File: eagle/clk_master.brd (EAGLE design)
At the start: 76.2 x 50.8 mm, 68 parts

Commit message: update eagle files
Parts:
- renumbered E$1 to R13, E$11 to U4, E$12 to J1, E$13 to C1, E$14 to C2, E$15 to C3, E$16 to C4, E$17 to R1, E$18 to R2, E$19 to R3, E$2 to U3, E$20 to R4, E$21 to C5, E$22 to U7, E$23 to C26, E$24 to C25, E$25 to R15, E$26 to R14, E$27 to C27, E$28 to U6, E$29 to C29, E$3 to U9, E$30 to C28, E$31 to J2, E$32 to C13, E$33 to L1, E$34 to C14, E$35 to C31, E$36 to C30, E$37 to C6, E$38 to C9, E$39 to C7, E$4 to U2, E$40 to C8, E$41 to C10, E$42 to C17, E$43 to C11, E$44 to C12, E$45 to C18, E$47 to C19, E$48 to C15, E$49 to D2, E$5 to U8, E$50 to D1, E$51 to R5, E$52 to R6, E$53 to C22, E$54 to L3, E$55 to C23, E$56 to U5, E$57 to C24, E$58 to PDI, E$59 to R8, E$6 to U1, E$60 to R7, E$61 to R10, E$62 to R9, E$63 to C20, E$64 to C21, E$65 to L2, E$66 to C16, E$67 to R11, E$68 to R12
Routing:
- net GND: track 120.0 -> 121.0 mm

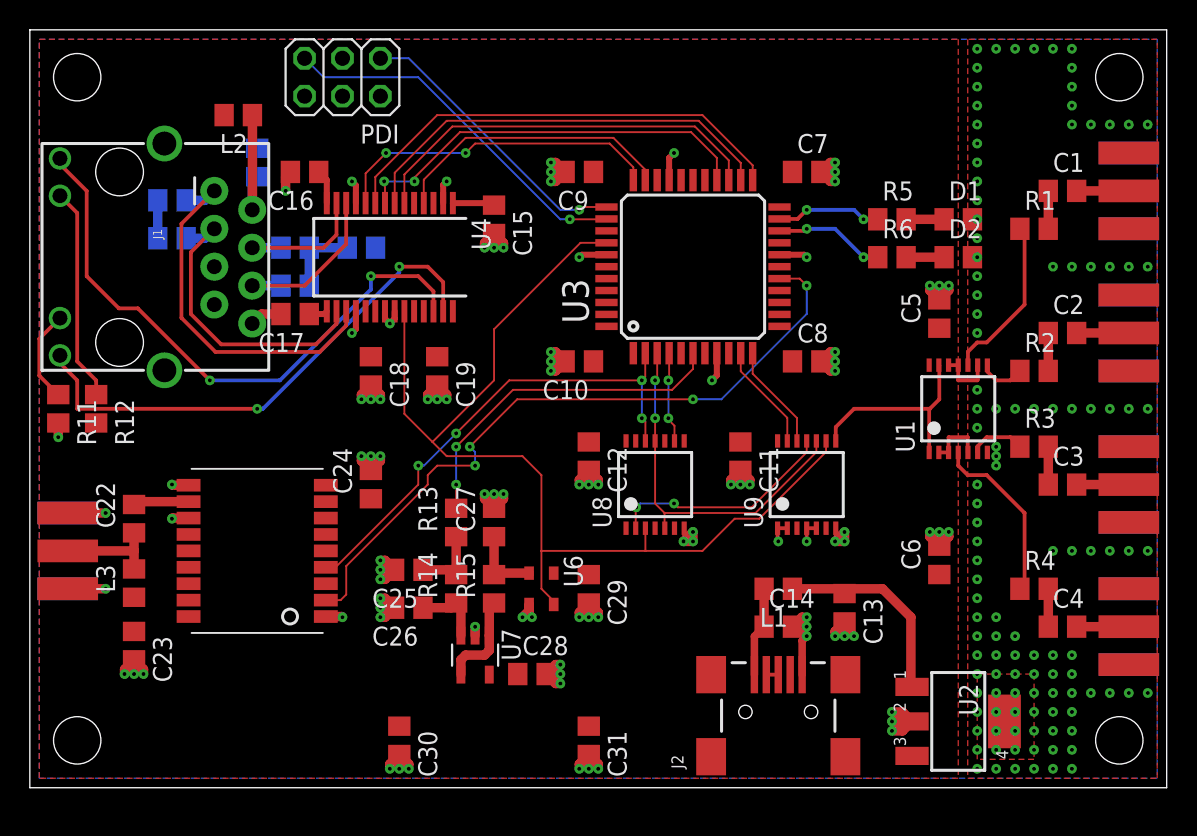
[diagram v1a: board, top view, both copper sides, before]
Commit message: clean up master clock board layout
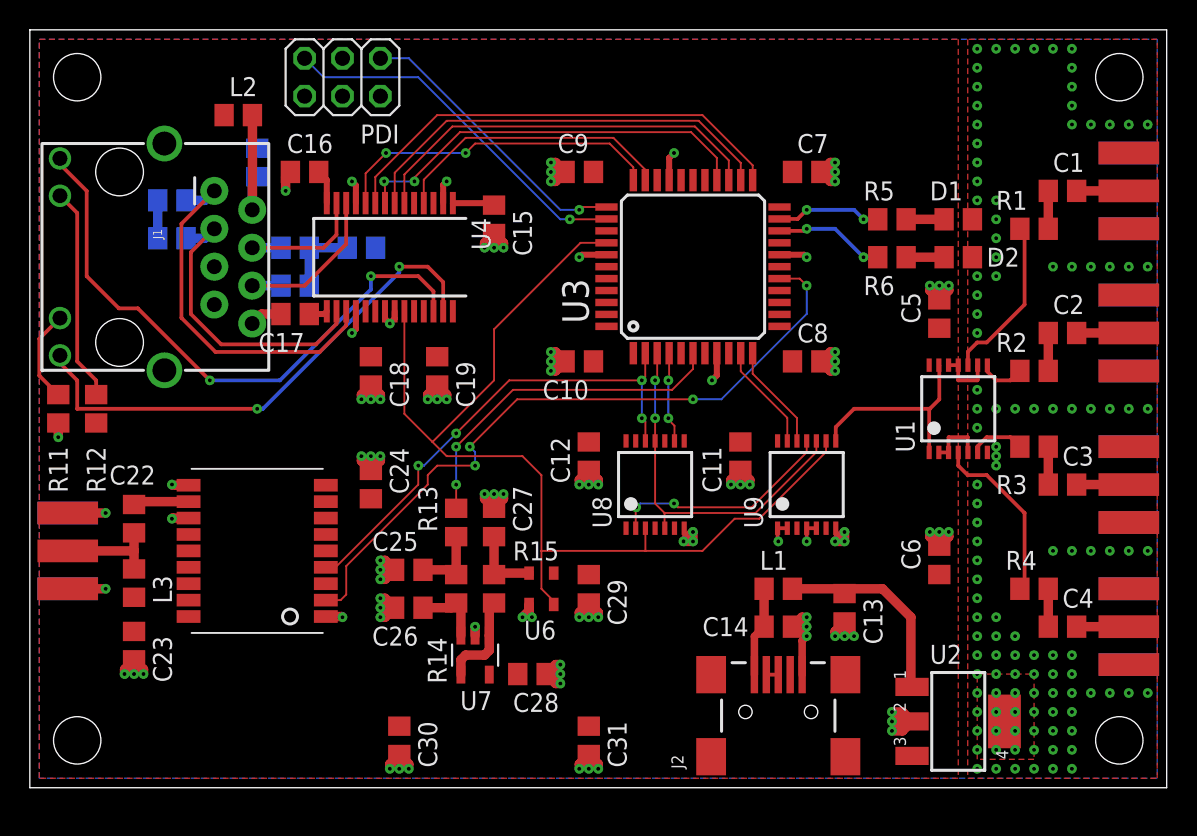
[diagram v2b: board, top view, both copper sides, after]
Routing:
- net GND: vias 209 -> 211

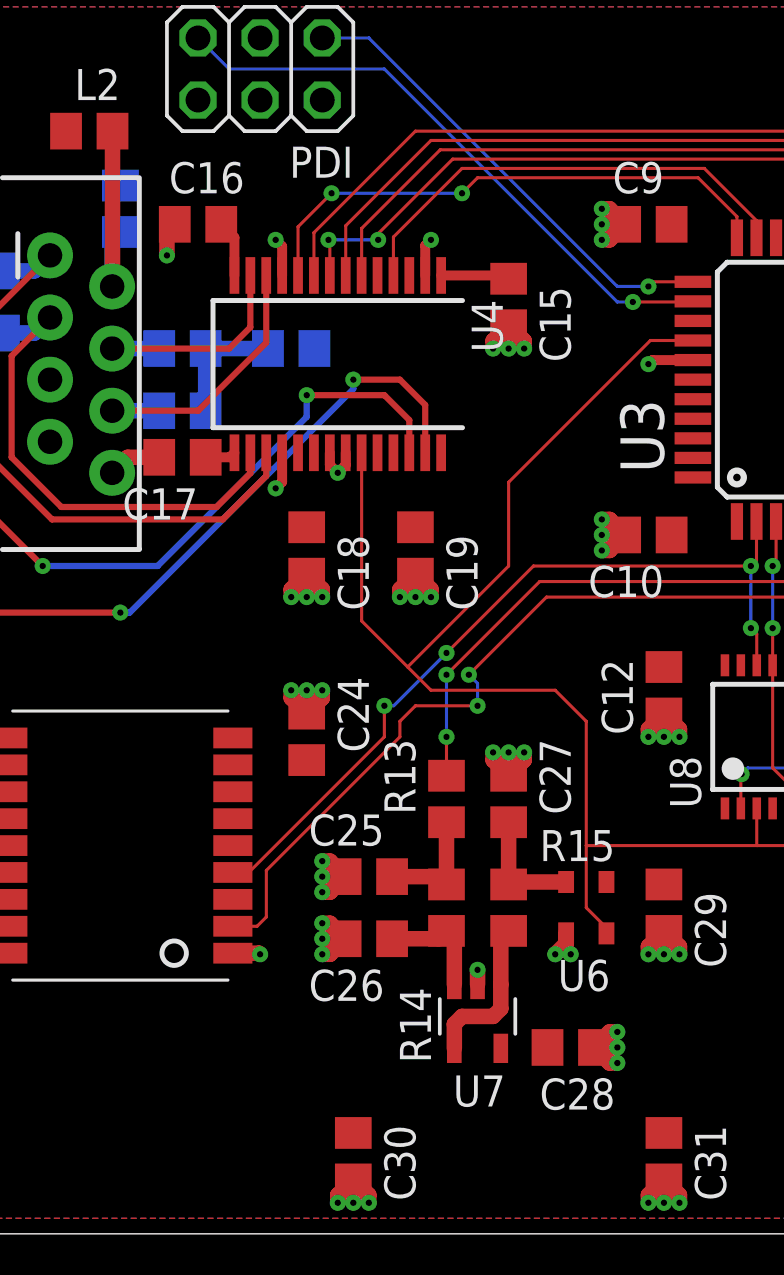
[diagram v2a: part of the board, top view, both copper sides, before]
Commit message: cleanup master clock layout
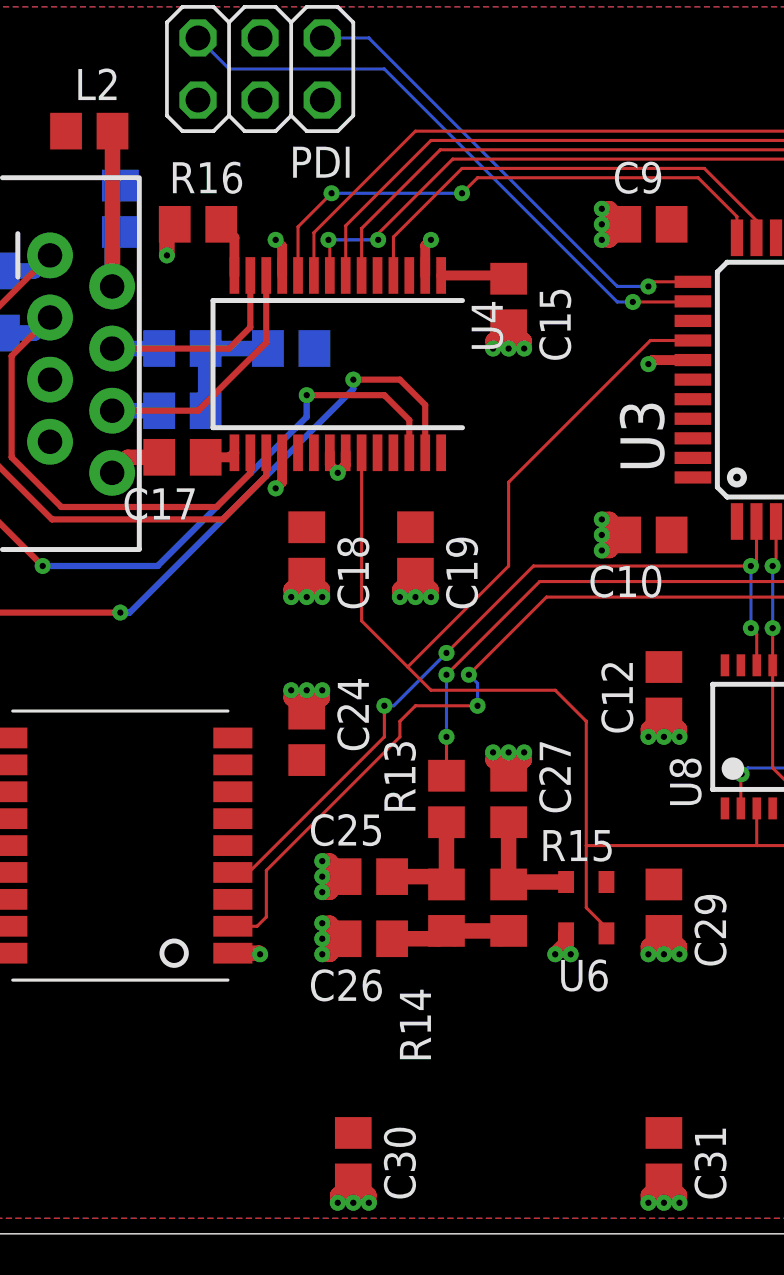
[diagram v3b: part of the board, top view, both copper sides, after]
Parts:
- removed C28: (no value), rcl:R0805
- removed U7: (no value), linear:SOT23-5
- renumbered C16 to R16
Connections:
- removed net S$19: R15.1, U7.1, U7.4
- net GND: no longer C28.2, U7.2
- net S$16: now also R15.1; no longer U7.3
- net V3.3: no longer C28.1, U7.5
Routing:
- net S$19: track 6.46 -> 0.00 mm
- net GND: track 121.0 -> 117.0 mm, vias 211 -> 207
- net S$16: track 4.68 -> 5.80 mm
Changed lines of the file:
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@@
 <attribute name="VALUE" x="63.5" y="31.115" size="1.27" layer="27" rot="R90"/>
-</element>
-<element name="U7" library="linear" library_urn="urn:adsk.eagle:library:262" package="SOT23-5" package3d_urn="urn:adsk.eagle:package:16456/2" value="" x="29.845" y="8.89" smashed="yes" rot="R180">
-<attribute name="NAME" x="30.988" y="6.477" size="1.27" layer="25" ratio="10" rot="R180"/>
-<attribute name="VALUE" x="26.797" y="10.668" size="1.27" layer="27" ratio="10" rot="R270"/>
 </element>
 <element name="C26" library="rcl" library_urn="urn:adsk.eagle:library:334" package="R0805" package3d_urn="urn:adsk.eagle:package:23553/2" value="" x="25.4" y="12.065" smashed="yes" rot="R180">
@@
 <attribute name="NAME" x="38.735" y="13.97" size="1.27" layer="25" rot="R270"/>
 <attribute name="VALUE" x="34.925" y="13.97" size="1.27" layer="27" rot="R270"/>
-</element>
-<element name="C28" library="rcl" library_urn="urn:adsk.eagle:library:334" package="R0805" package3d_urn="urn:adsk.eagle:package:23553/2" value="" x="33.655" y="7.62" smashed="yes">
-<attribute name="NAME" x="32.385" y="5.08" size="1.27" layer="25"/>
-<attribute name="VALUE" x="33.02" y="5.08" size="1.27" layer="27"/>
 </element>
 <element name="J2" library="SparkFun-Connectors" library_urn="urn:adsk.eagle:library:513" package="USB-MINIB" package3d_urn="urn:adsk.eagle:package:38244/1" value="" x="50.165" y="5.08" smashed="yes" rot="R90">
@@
 <attribute name="VALUE" x="14.605" y="47.625" size="1.27" layer="27" rot="R180"/>
 </element>
-<element name="C16" library="rcl" library_urn="urn:adsk.eagle:library:334" package="R0805" package3d_urn="urn:adsk.eagle:package:23553/2" value="" x="18.415" y="41.275" smashed="yes" rot="R180">
+<element name="R16" library="rcl" library_urn="urn:adsk.eagle:library:334" package="R0805" package3d_urn="urn:adsk.eagle:package:23553/2" value="" x="18.415" y="41.275" smashed="yes" rot="R180">
 <attribute name="NAME" x="20.32" y="43.815" size="1.27" layer="25" rot="R180"/>
 <attribute name="VALUE" x="19.05" y="43.815" size="1.27" layer="27" rot="R180"/>
@@
 <contactref element="C29" pad="1"/>
 <contactref element="U6" pad="4"/>
-<contactref element="U7" pad="5"/>
-<contactref element="C28" pad="1"/>
 <contactref element="U2" pad="3"/>
 <contactref element="C30" pad="1"/>
@@
 <wire x1="31.115" y1="18.73" x2="31.75" y2="19.365" width="0.635" layer="1"/>
 <wire x1="31.75" y1="19.365" x2="31.75" y2="19.685" width="0.635" layer="1"/>
-<via x="29.845" y="10.795" extent="1-16" drill="0.254"/>
-<contactref element="U7" pad="2"/>
-<wire x1="29.845" y1="10.196" x2="29.845" y2="10.795" width="0.635" layer="1"/>
-<contactref element="C28" pad="2"/>
-<via x="35.56" y="8.255" extent="1-16" drill="0.254"/>
-<via x="35.56" y="7.62" extent="1-16" drill="0.254"/>
-<via x="35.56" y="6.985" extent="1-16" drill="0.254"/>
-<wire x1="34.605" y1="7.62" x2="35.56" y2="7.62" width="0.635" layer="1"/>
-<wire x1="34.605" y1="7.62" x2="35.24" y2="8.255" width="0.635" layer="1"/>
-<wire x1="35.24" y1="8.255" x2="35.56" y2="8.255" width="0.635" layer="1"/>
-<wire x1="34.605" y1="7.62" x2="35.24" y2="6.985" width="0.635" layer="1"/>
-<wire x1="35.24" y1="6.985" x2="35.56" y2="6.985" width="0.635" layer="1"/>
 <contactref element="U2" pad="4"/>
 <contactref element="U2" pad="2"/>
@@
 <contactref element="C21" pad="2"/>
 <via x="17.145" y="40.005" extent="1-16" drill="0.254"/>
-<contactref element="C16" pad="2"/>
+<contactref element="R16" pad="2"/>
 <wire x1="17.465" y1="41.275" x2="17.145" y2="40.955" width="0.635" layer="1"/>
 <wire x1="17.145" y1="40.955" x2="17.145" y2="40.005" width="0.635" layer="1"/>
@@
 <wire x1="26.35" y1="12.065" x2="28.255" y2="12.065" width="0.635" layer="1"/>
 <wire x1="28.255" y1="12.065" x2="28.575" y2="12.385" width="0.635" layer="1"/>
-<contactref element="U7" pad="3"/>
-<wire x1="28.895" y1="10.196" x2="28.895" y2="12.065" width="0.635" layer="1"/>
 <wire x1="28.895" y1="12.065" x2="28.575" y2="12.385" width="0.635" layer="1"/>
+<contactref element="R15" pad="1"/>
+<wire x1="30.795" y1="12.065" x2="31.115" y2="12.385" width="0.635" layer="1"/>
+<wire x1="28.575" y1="12.385" x2="31.115" y2="12.385" width="0.635" layer="1"/>
 </signal>
 <signal name="S$17">
@@
 <wire x1="31.215" y1="14.385" x2="31.115" y2="14.285" width="0.635" layer="1"/>
 <wire x1="31.115" y1="16.83" x2="31.115" y2="14.285" width="0.635" layer="1"/>
-</signal>
-<signal name="S$19">
-<contactref element="U7" pad="1"/>
-<contactref element="U7" pad="4"/>
-<contactref element="R15" pad="1"/>
-<wire x1="30.795" y1="10.196" x2="30.795" y2="12.065" width="0.635" layer="1"/>
-<wire x1="30.795" y1="12.065" x2="31.115" y2="12.385" width="0.635" layer="1"/>
-<wire x1="30.795" y1="10.196" x2="30.795" y2="9.205" width="0.635" layer="1"/>
-<wire x1="30.48" y1="8.89" x2="30.795" y2="9.205" width="0.635" layer="1"/>
-<wire x1="28.895" y1="7.584" x2="28.895" y2="8.575" width="0.635" layer="1"/>
-<wire x1="28.895" y1="8.575" x2="29.21" y2="8.89" width="0.635" layer="1"/>
-<wire x1="29.21" y1="8.89" x2="30.48" y2="8.89" width="0.635" layer="1"/>
 </signal>
 <signal name="S$20">
@@
 <signal name="S$53">
 <contactref element="U4" pad="14"/>
-<contactref element="C16" pad="1"/>
+<contactref element="R16" pad="1"/>
 <wire x1="19.905" y1="39.185" x2="19.905" y2="40.735" width="0.4064" layer="1"/>
 <wire x1="19.905" y1="40.735" x2="19.365" y2="41.275" width="0.4064" layer="1"/>

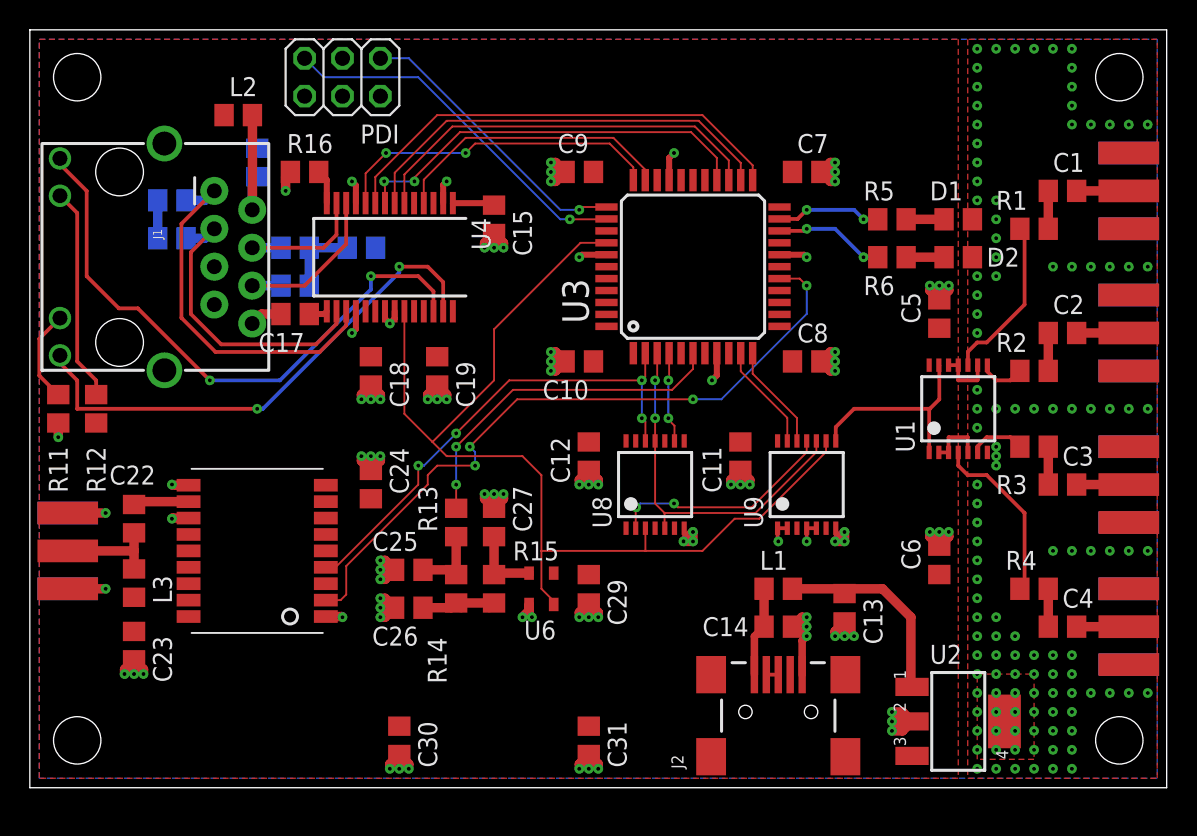
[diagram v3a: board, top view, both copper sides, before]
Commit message: add master clock component values
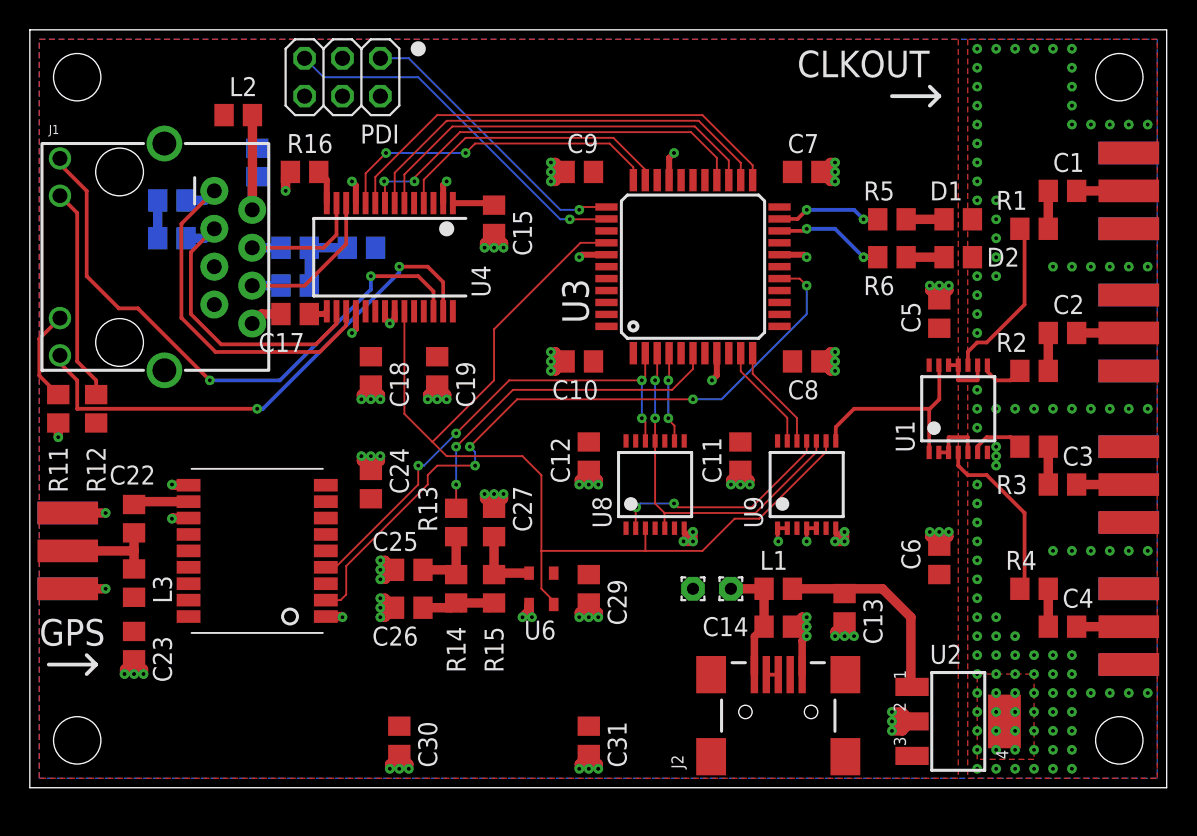
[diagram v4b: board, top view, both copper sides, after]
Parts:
- added E$1, E$2: (no value), wirepad:1,6/0,8
- C1, C2, C22, C3, C4: value (none) -> 47n
- C10, C11, C12, C14, C17, C18, C19, C20, C23, C24, C25, C27, C29, C5, C6, C7, C8, C9: value (none) -> 100n
- C13, C26, C30, C31: value (none) -> 100u
- C15, L1, L2: value (none) -> 10u
- L3: value (none) -> 22n
- R1, R10, R2, R3, R4, R7, R8, R9: value (none) -> 49.9
- R11, R12, R13, R15, R5, R6: value (none) -> 330
- R14: value (none) -> 10k
- R16: value (none) -> 2.32k
- U1: value (none) -> 74LVCU04A
- U2: value (none) -> MCP1824ST-3302E
- U3: value (none) -> ATXMEGA16A4U
- U4: value (none) -> ENC28J60
- U5: value (none) -> TESEO-LIV3R
- U8: value (none) -> 74LVC74A
- U9: value (none) -> 74LVC86A
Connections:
- net S$21 renamed V5
- removed net S$20: C14.1, J2.VBUS, L1.2
- new net VBUS: C14.1, E$1.1, J2.VBUS, L1.2
- net GND: now also E$2.1
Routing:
- net VBUS: track 0.00 -> 8.25 mm
- net S$20: track 6.02 -> 0.00 mm
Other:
- board text added: "CLKOUT"
- board text added: "GPS"
